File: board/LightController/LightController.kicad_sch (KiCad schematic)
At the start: 34 parts, among them J1 PJ-051AH, J2 Light bank 1, J3 Light Bank 2, J4 Light Bank 3, U1 CPC1002N, U10 CPC1002N, U11 CPC1002N, U12 FeatherS2, U2 CPC1002N, U3 CPC1002N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

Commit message: Add test points.
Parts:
- added TP1: 24V, TestPoint:TestPoint_Pad_D4.0mm, symbol Connector:TestPoint
- added TP2: GND, TestPoint:TestPoint_Loop_D2.54mm_Drill1.5mm_Beaded, symbol Connector:TestPoint
- added TP3: 5V, TestPoint:TestPoint_Pad_D4.0mm, symbol Connector:TestPoint
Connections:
- net +24V: now also TP1.1
- net +5V: now also TP3.1
- net GND: now also TP2.1
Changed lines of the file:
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@@
   (junction (at 44.45 41.91) (diameter 0) (color 0 0 0 0)
   )
+  (junction (at 93.98 59.69) (diameter 0) (color 0 0 0 0)
+  )
   (junction (at 113.03 44.45) (diameter 0) (color 0 0 0 0)
   )
@@
   (junction (at 109.22 44.45) (diameter 0) (color 0 0 0 0)
   )
+  (junction (at 52.07 41.91) (diameter 0) (color 0 0 0 0)
+  )
   (junction (at 87.63 44.45) (diameter 0) (color 0 0 0 0)
+  )
+  (junction (at 116.84 44.45) (diameter 0) (color 0 0 0 0)
   )
   (junction (at 68.58 59.69) (diameter 0) (color 0 0 0 0)
@@
     (stroke (width 0) (type default) (color 0 0 0 0))
   )
+  (wire (pts (xy 52.07 41.91) (xy 54.61 41.91))
+    (stroke (width 0) (type default) (color 0 0 0 0))
+  )
   (wire (pts (xy 109.22 44.45) (xy 109.22 46.99))
     (stroke (width 0) (type default) (color 0 0 0 0))
@@
     (stroke (width 0) (type default) (color 0 0 0 0))
   )
-  (wire (pts (xy 113.03 59.69) (xy 76.2 59.69))
+  (wire (pts (xy 113.03 59.69) (xy 93.98 59.69))
     (stroke (width 0) (type default) (color 0 0 0 0))
   )
@@
     (stroke (width 0) (type default) (color 0 0 0 0))
   )
+  (wire (pts (xy 93.98 59.69) (xy 76.2 59.69))
+    (stroke (width 0) (type default) (color 0 0 0 0))
+  )
   (wire (pts (xy 222.25 92.71) (xy 231.14 92.71))
     (stroke (width 0) (type default) (color 0 0 0 0))
@@
     (stroke (width 0) (type default) (color 0 0 0 0))
   )
-  (wire (pts (xy 113.03 44.45) (xy 123.19 44.45))
+  (wire (pts (xy 113.03 44.45) (xy 116.84 44.45))
     (stroke (width 0) (type default) (color 0 0 0 0))
   )
@@
     (stroke (width 0) (type default) (color 0 0 0 0))
   )
-  (wire (pts (xy 48.26 41.91) (xy 54.61 41.91))
+  (wire (pts (xy 48.26 41.91) (xy 52.07 41.91))
     (stroke (width 0) (type default) (color 0 0 0 0))
   )
@@
   )
   (wire (pts (xy 257.175 55.88) (xy 259.08 55.88))
+    (stroke (width 0) (type default) (color 0 0 0 0))
+  )
+  (wire (pts (xy 116.84 44.45) (xy 123.19 44.45))
     (stroke (width 0) (type default) (color 0 0 0 0))
   )
@@
   (symbol (lib_id "power:GND") (at 240.03 32.385 0) (unit 1)
     (in_bom yes) (on_board yes) (fields_autoplaced)
-    (property "Reference" "#PWR026" (id 0) (at 240.03 38.735 0)
+    (property "Reference" "#PWR027" (id 0) (at 240.03 38.735 0)
       (effects (font (size 1.27 1.27)) hide)
     )
@@
     (pin "2")
   )
+  (symbol (lib_id "Connector:TestPoint") (at 52.07 41.91 0) (unit 1)
+    (in_bom yes) (on_board yes)
+    (property "Reference" "TP1" (id 0) (at 50.8 34.29 0)
+      (effects (font (size 1.27 1.27)) (justify left))
+    )
+    (property "Value" "24V" (id 1) (at 50.8 36.83 0)
+      (effects (font (size 1.27 1.27)) (justify left))
+    )
+    (property "Footprint" "TestPoint:TestPoint_Pad_D4.0mm" (id 2) (at 57.15 41.91 0)
+      (effects (font (size 1.27 1.27)) hide)
+    )
+    (property "Datasheet" "~" (id 3) (at 57.15 41.91 0)
+      (effects (font (size 1.27 1.27)) hide)
+    )
+    (pin "1")
+  )
   (symbol (lib_id "power:GND") (at 21.59 182.88 0) (unit 1)
     (in_bom yes) (on_board yes) (fields_autoplaced)
@@
     )
     (property "Datasheet" "" (id 3) (at 231.14 90.17 0)
+      (effects (font (size 1.27 1.27)) hide)
+    )
+    (pin "1")
+  )
+  (symbol (lib_id "Connector:TestPoint") (at 116.84 44.45 0) (unit 1)
+    (in_bom yes) (on_board yes)
+    (property "Reference" "TP3" (id 0) (at 114.046 36.068 0)
+      (effects (font (size 1.27 1.27)) (justify left))
+    )
+    (property "Value" "5V" (id 1) (at 111.252 38.862 0)
+      (effects (font (size 1.27 1.27)) (justify left))
+    )
+    (property "Footprint" "TestPoint:TestPoint_Pad_D4.0mm" (id 2) (at 121.92 44.45 0)
+      (effects (font (size 1.27 1.27)) hide)
+    )
+    (property "Datasheet" "~" (id 3) (at 121.92 44.45 0)
       (effects (font (size 1.27 1.27)) hide)
     )
@@
   (symbol (lib_id "power:GND") (at 240.665 51.435 0) (unit 1)
     (in_bom yes) (on_board yes) (fields_autoplaced)
-    (property "Reference" "#PWR027" (id 0) (at 240.665 57.785 0)
+    (property "Reference" "#PWR028" (id 0) (at 240.665 57.785 0)
       (effects (font (size 1.27 1.27)) hide)
     )
@@
     )
   )
+  (symbol (lib_id "Connector:TestPoint") (at 93.98 59.69 0) (unit 1)
+    (in_bom yes) (on_board yes) (fields_autoplaced)
+    (property "Reference" "TP2" (id 0) (at 96.52 55.1179 0)
+      (effects (font (size 1.27 1.27)) (justify left))
+    )
+    (property "Value" "GND" (id 1) (at 96.52 57.6579 0)
+      (effects (font (size 1.27 1.27)) (justify left))
+    )
+    (property "Footprint" "TestPoint:TestPoint_Loop_D2.54mm_Drill1.5mm_Beaded" (id 2) (at 99.06 59.69 0)
+      (effects (font (size 1.27 1.27)) hide)
+    )
+    (property "Datasheet" "~" (id 3) (at 99.06 59.69 0)
+      (effects (font (size 1.27 1.27)) hide)
+    )
+    (pin "1")
+  )
   (symbol (lib_id "power:GND") (at 238.125 69.215 0) (unit 1)
     (in_bom yes) (on_board yes) (fields_autoplaced)
-    (property "Reference" "#PWR028" (id 0) (at 238.125 75.565 0)
+    (property "Reference" "#PWR026" (id 0) (at 238.125 75.565 0)
       (effects (font (size 1.27 1.27)) hide)
     )
@@
       (reference "#PWR025") (unit 1) (value "+5V") (footprint "")
     )
+    (path "/ffaa8227-6a33-4a9e-b9b1-1fd1b243401f"
+      (reference "#PWR026") (unit 1) (value "GND") (footprint "")
+    )
     (path "/118363d9-1248-4653-9b45-ceb5f08f9daf"
-      (reference "#PWR026") (unit 1) (value "GND") (footprint "")
+      (reference "#PWR027") (unit 1) (value "GND") (footprint "")
     )
     (path "/7219b893-260e-4790-8a1d-0a840f6f2a4d"
-      (reference "#PWR027") (unit 1) (value "GND") (footprint "")
-    )
-    (path "/ffaa8227-6a33-4a9e-b9b1-1fd1b243401f"
       (reference "#PWR028") (unit 1) (value "GND") (footprint "")
     )
@@
       (reference "R10") (unit 1) (value "3K3") (footprint "Resistor_SMD:R_0805_2012Metric")
     )
+    (path "/25f413c1-7149-4b14-bcd6-9f919a841766"
+      (reference "TP1") (unit 1) (value "24V") (footprint "TestPoint:TestPoint_Pad_D4.0mm")
+    )
+    (path "/ff579e34-65c1-4f50-a33e-b27af09e16ee"
+      (reference "TP2") (unit 1) (value "GND") (footprint "TestPoint:TestPoint_Loop_D2.54mm_Drill1.5mm_Beaded")
+    )
+    (path "/46eb0307-3674-45bc-a7fe-d6adb29b2149"
+      (reference "TP3") (unit 1) (value "5V") (footprint "TestPoint:TestPoint_Pad_D4.0mm")
+    )
     (path "/8f2e333e-0bdc-409e-a046-778d2c85a608"

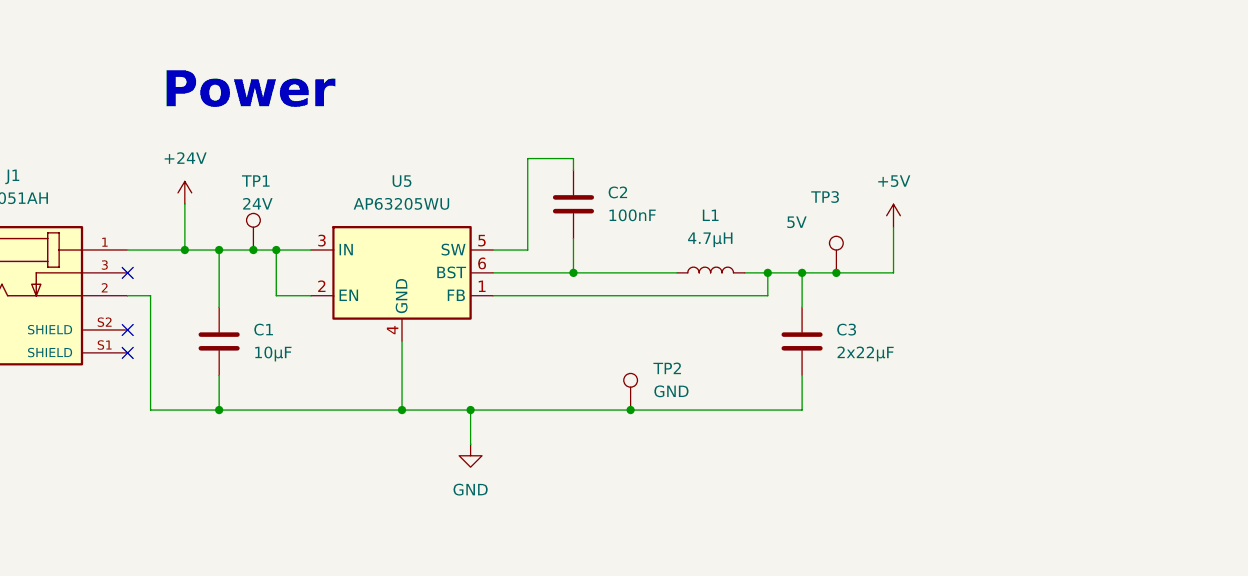
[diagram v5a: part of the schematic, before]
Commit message: Added second parallel bypass cap.
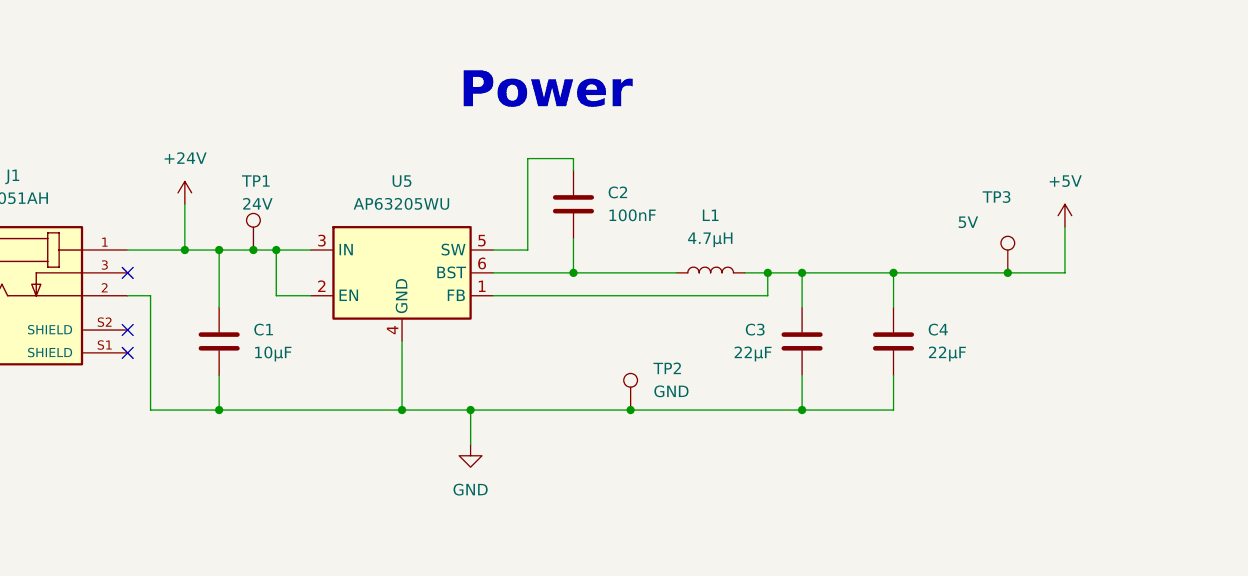
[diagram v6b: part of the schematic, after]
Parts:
- added C4: 22µF, Capacitor_SMD:C_0805_2012Metric, symbol Device:C
- C3: value 2x22µF -> 22µF
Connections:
- net +5V: now also C4.1
- net GND: now also C4.2
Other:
- moved on the sheet: TP3
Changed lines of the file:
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@@
   (junction (at 93.98 59.69) (diameter 0) (color 0 0 0 0)
   )
+  (junction (at 48.26 41.91) (diameter 0) (color 0 0 0 0)
+  )
   (junction (at 113.03 44.45) (diameter 0) (color 0 0 0 0)
   )
-  (junction (at 48.26 41.91) (diameter 0) (color 0 0 0 0)
-  )
   (junction (at 109.22 44.45) (diameter 0) (color 0 0 0 0)
   )
@@
   (junction (at 87.63 44.45) (diameter 0) (color 0 0 0 0)
   )
-  (junction (at 116.84 44.45) (diameter 0) (color 0 0 0 0)
+  (junction (at 113.03 59.69) (diameter 0) (color 0 0 0 0)
+  )
+  (junction (at 135.89 44.45) (diameter 0) (color 0 0 0 0)
   )
   (junction (at 68.58 59.69) (diameter 0) (color 0 0 0 0)
+  )
+  (junction (at 123.19 44.45) (diameter 0) (color 0 0 0 0)
   )
   (junction (at 48.26 59.69) (diameter 0) (color 0 0 0 0)
@@
     (stroke (width 0) (type default) (color 0 0 0 0))
   )
+  (wire (pts (xy 123.19 59.69) (xy 113.03 59.69))
+    (stroke (width 0) (type default) (color 0 0 0 0))
+  )
   (wire (pts (xy 44.45 36.83) (xy 44.45 41.91))
     (stroke (width 0) (type default) (color 0 0 0 0))
@@
     (stroke (width 0) (type default) (color 0 0 0 0))
   )
+  (wire (pts (xy 123.19 55.88) (xy 123.19 59.69))
+    (stroke (width 0) (type default) (color 0 0 0 0))
+  )
   (wire (pts (xy 44.45 41.91) (xy 48.26 41.91))
     (stroke (width 0) (type default) (color 0 0 0 0))
@@
     (stroke (width 0) (type default) (color 0 0 0 0))
   )
+  (wire (pts (xy 123.19 44.45) (xy 123.19 48.26))
+    (stroke (width 0) (type default) (color 0 0 0 0))
+  )
   (wire (pts (xy 257.175 69.85) (xy 259.08 69.85))
     (stroke (width 0) (type default) (color 0 0 0 0))
@@
     (stroke (width 0) (type default) (color 0 0 0 0))
   )
-  (wire (pts (xy 123.19 39.37) (xy 123.19 44.45))
+  (wire (pts (xy 142.24 39.37) (xy 142.24 44.45))
     (stroke (width 0) (type default) (color 0 0 0 0))
   )
@@
     (stroke (width 0) (type default) (color 0 0 0 0))
   )
-  (wire (pts (xy 113.03 44.45) (xy 116.84 44.45))
+  (wire (pts (xy 113.03 44.45) (xy 123.19 44.45))
     (stroke (width 0) (type default) (color 0 0 0 0))
   )
@@
     (stroke (width 0) (type default) (color 0 0 0 0))
   )
-  (wire (pts (xy 116.84 44.45) (xy 123.19 44.45))
+  (wire (pts (xy 135.89 44.45) (xy 142.24 44.45))
     (stroke (width 0) (type default) (color 0 0 0 0))
   )
@@
   )
   (wire (pts (xy 22.225 160.655) (xy 22.225 161.29))
+    (stroke (width 0) (type default) (color 0 0 0 0))
+  )
+  (wire (pts (xy 123.19 44.45) (xy 135.89 44.45))
     (stroke (width 0) (type default) (color 0 0 0 0))
   )
@@
     (effects (font (size 4 4) (thickness 0.8) bold) (justify left bottom))
   )
-  (text "Power" (at 41.91 26.67 0)
+  (text "Power" (at 74.93 26.67 0)
     (effects (font (size 4 4) (thickness 0.8) bold) (justify left bottom))
   )
@@
   )
   (symbol (lib_id "Device:C") (at 113.03 52.07 0) (unit 1)
-    (in_bom yes) (on_board yes) (fields_autoplaced)
-    (property "Reference" "C3" (id 0) (at 116.84 50.7999 0)
-      (effects (font (size 1.27 1.27)) (justify left))
-    )
-    (property "Value" "2x22µF" (id 1) (at 116.84 53.3399 0)
+    (in_bom yes) (on_board yes)
+    (property "Reference" "C3" (id 0) (at 106.68 50.8 0)
+      (effects (font (size 1.27 1.27)) (justify left))
+    )
+    (property "Value" "22µF" (id 1) (at 105.41 53.34 0)
       (effects (font (size 1.27 1.27)) (justify left))
     )
@@
     (pin "1")
   )
-  (symbol (lib_id "Connector:TestPoint") (at 116.84 44.45 0) (unit 1)
+  (symbol (lib_id "Connector:TestPoint") (at 135.89 44.45 0) (unit 1)
     (in_bom yes) (on_board yes)
-    (property "Reference" "TP3" (id 0) (at 114.046 36.068 0)
-      (effects (font (size 1.27 1.27)) (justify left))
-    )
-    (property "Value" "5V" (id 1) (at 111.252 38.862 0)
-      (effects (font (size 1.27 1.27)) (justify left))
-    )
-    (property "Footprint" "TestPoint:TestPoint_Pad_D4.0mm" (id 2) (at 121.92 44.45 0)
-      (effects (font (size 1.27 1.27)) hide)
-    )
-    (property "Datasheet" "~" (id 3) (at 121.92 44.45 0)
+    (property "Reference" "TP3" (id 0) (at 133.096 36.068 0)
+      (effects (font (size 1.27 1.27)) (justify left))
+    )
+    (property "Value" "5V" (id 1) (at 130.302 38.862 0)
+      (effects (font (size 1.27 1.27)) (justify left))
+    )
+    (property "Footprint" "TestPoint:TestPoint_Pad_D4.0mm" (id 2) (at 140.97 44.45 0)
+      (effects (font (size 1.27 1.27)) hide)
+    )
+    (property "Datasheet" "~" (id 3) (at 140.97 44.45 0)
       (effects (font (size 1.27 1.27)) hide)
     )
@@
     (pin "1")
   )
-  (symbol (lib_id "power:+5V") (at 123.19 39.37 0) (unit 1)
-    (in_bom yes) (on_board yes) (fields_autoplaced)
-    (property "Reference" "#PWR020" (id 0) (at 123.19 43.18 0)
-      (effects (font (size 1.27 1.27)) hide)
-    )
-    (property "Value" "+5V" (id 1) (at 123.19 34.29 0))
-    (property "Footprint" "" (id 2) (at 123.19 39.37 0)
-      (effects (font (size 1.27 1.27)) hide)
-    )
-    (property "Datasheet" "" (id 3) (at 123.19 39.37 0)
+  (symbol (lib_id "power:+5V") (at 142.24 39.37 0) (unit 1)
+    (in_bom yes) (on_board yes) (fields_autoplaced)
+    (property "Reference" "#PWR020" (id 0) (at 142.24 43.18 0)
+      (effects (font (size 1.27 1.27)) hide)
+    )
+    (property "Value" "+5V" (id 1) (at 142.24 34.29 0))
+    (property "Footprint" "" (id 2) (at 142.24 39.37 0)
+      (effects (font (size 1.27 1.27)) hide)
+    )
+    (property "Datasheet" "" (id 3) (at 142.24 39.37 0)
       (effects (font (size 1.27 1.27)) hide)
     )
@@
       (effects (font (size 1.27 1.27)) hide)
     )
+  )
+  (symbol (lib_id "Device:C") (at 123.19 52.07 0) (unit 1)
+    (in_bom yes) (on_board yes) (fields_autoplaced)
+    (property "Reference" "C4" (id 0) (at 127 50.7999 0)
+      (effects (font (size 1.27 1.27)) (justify left))
+    )
+    (property "Value" "22µF" (id 1) (at 127 53.3399 0)
+      (effects (font (size 1.27 1.27)) (justify left))
+    )
+    (property "Footprint" "Capacitor_SMD:C_0805_2012Metric" (id 2) (at 124.1552 55.88 0)
+      (effects (font (size 1.27 1.27)) hide)
+    )
+    (property "Datasheet" "~" (id 3) (at 123.19 52.07 0)
+      (effects (font (size 1.27 1.27)) hide)
+    )
+    (pin "1")
+    (pin "2")
   )
   (symbol (lib_id "Relay_SolidState:CPC1002N") (at 38.735 179.705 0) (unit 1)
@@
     )
     (path "/358be4dc-9ae7-42fb-bb5f-97253842315f"
-      (reference "C3") (unit 1) (value "2x22µF") (footprint "Capacitor_SMD:C_0805_2012Metric")
+      (reference "C3") (unit 1) (value "22µF") (footprint "Capacitor_SMD:C_0805_2012Metric")
+    )
+    (path "/8da86106-0751-4439-acdd-3f37b2dbfba6"
+      (reference "C4") (unit 1) (value "22µF") (footprint "Capacitor_SMD:C_0805_2012Metric")
     )
     (path "/5fdabda6-9c9c-427b-87e5-a291030a9854"

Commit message: fixed resistor label orientations.
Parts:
- L1: value 4.7µH -> 8.7µH
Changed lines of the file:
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@@
   (symbol (lib_id "Device:R") (at 76.835 137.16 90) (unit 1)
     (in_bom yes) (on_board yes)
-    (property "Reference" "R6" (id 0) (at 76.2 142.875 0)
-      (effects (font (size 1.27 1.27)) (justify left))
-    )
-    (property "Value" "3K3" (id 1) (at 78.105 142.875 0)
+    (property "Reference" "R6" (id 0) (at 78.74 139.7 90)
+      (effects (font (size 1.27 1.27)) (justify left))
+    )
+    (property "Value" "3K3" (id 1) (at 80.01 142.24 90)
       (effects (font (size 1.27 1.27)) (justify left))
     )
@@
   (symbol (lib_id "Device:R") (at 77.47 102.87 90) (unit 1)
     (in_bom yes) (on_board yes)
-    (property "Reference" "R7" (id 0) (at 76.835 108.585 0)
-      (effects (font (size 1.27 1.27)) (justify left))
-    )
-    (property "Value" "3K3" (id 1) (at 78.74 108.585 0)
+    (property "Reference" "R7" (id 0) (at 78.74 105.41 90)
+      (effects (font (size 1.27 1.27)) (justify left))
+    )
+    (property "Value" "3K3" (id 1) (at 80.01 107.95 90)
       (effects (font (size 1.27 1.27)) (justify left))
     )
@@
     (in_bom yes) (on_board yes) (fields_autoplaced)
     (property "Reference" "L1" (id 0) (at 102.87 38.1 90))
-    (property "Value" "4.7µH" (id 1) (at 102.87 40.64 90))
+    (property "Value" "8.7µH" (id 1) (at 102.87 40.64 90))
     (property "Footprint" "Inductor_SMD:L_0805_2012Metric" (id 2) (at 102.87 44.45 0)
       (effects (font (size 1.27 1.27)) hide)
@@
   (symbol (lib_id "Device:R") (at 124.46 161.925 90) (unit 1)
     (in_bom yes) (on_board yes)
-    (property "Reference" "R8" (id 0) (at 123.825 167.64 0)
-      (effects (font (size 1.27 1.27)) (justify left))
-    )
-    (property "Value" "3K3" (id 1) (at 125.73 167.64 0)
+    (property "Reference" "R8" (id 0) (at 127 165.1 90)
+      (effects (font (size 1.27 1.27)) (justify left))
+    )
+    (property "Value" "3K3" (id 1) (at 128.27 167.64 90)
       (effects (font (size 1.27 1.27)) (justify left))
     )
@@
   (symbol (lib_id "Device:R") (at 76.2 161.925 90) (unit 1)
     (in_bom yes) (on_board yes)
-    (property "Reference" "R5" (id 0) (at 75.565 167.64 0)
-      (effects (font (size 1.27 1.27)) (justify left))
-    )
-    (property "Value" "3K3" (id 1) (at 77.47 167.64 0)
+    (property "Reference" "R5" (id 0) (at 78.74 165.1 90)
+      (effects (font (size 1.27 1.27)) (justify left))
+    )
+    (property "Value" "3K3" (id 1) (at 80.01 167.64 90)
       (effects (font (size 1.27 1.27)) (justify left))
     )
@@
   (symbol (lib_id "Device:R") (at 125.095 137.16 90) (unit 1)
     (in_bom yes) (on_board yes)
-    (property "Reference" "R9" (id 0) (at 124.46 142.875 0)
-      (effects (font (size 1.27 1.27)) (justify left))
-    )
-    (property "Value" "3K3" (id 1) (at 126.365 142.875 0)
+    (property "Reference" "R9" (id 0) (at 127 139.7 90)
+      (effects (font (size 1.27 1.27)) (justify left))
+    )
+    (property "Value" "3K3" (id 1) (at 128.27 142.24 90)
       (effects (font (size 1.27 1.27)) (justify left))
     )
@@
   (symbol (lib_id "Device:R") (at 26.67 160.655 90) (unit 1)
     (in_bom yes) (on_board yes)
-    (property "Reference" "R2" (id 0) (at 26.035 166.37 0)
-      (effects (font (size 1.27 1.27)) (justify left))
-    )
-    (property "Value" "3K3" (id 1) (at 27.94 166.37 0)
+    (property "Reference" "R2" (id 0) (at 27.94 163.83 90)
+      (effects (font (size 1.27 1.27)) (justify left))
+    )
+    (property "Value" "3K3" (id 1) (at 29.21 166.37 90)
       (effects (font (size 1.27 1.27)) (justify left))
     )
@@
   (symbol (lib_id "Device:R") (at 27.305 135.89 90) (unit 1)
     (in_bom yes) (on_board yes)
-    (property "Reference" "R3" (id 0) (at 26.67 141.605 0)
-      (effects (font (size 1.27 1.27)) (justify left))
-    )
-    (property "Value" "3K3" (id 1) (at 28.575 141.605 0)
+    (property "Reference" "R3" (id 0) (at 29.21 138.43 90)
+      (effects (font (size 1.27 1.27)) (justify left))
+    )
+    (property "Value" "3K3" (id 1) (at 30.48 140.97 90)
       (effects (font (size 1.27 1.27)) (justify left))
     )
@@
   (symbol (lib_id "Device:R") (at 26.035 182.245 90) (unit 1)
     (in_bom yes) (on_board yes)
-    (property "Reference" "R1" (id 0) (at 25.4 187.96 0)
-      (effects (font (size 1.27 1.27)) (justify left))
-    )
-    (property "Value" "3K3" (id 1) (at 27.305 187.96 0)
+    (property "Reference" "R1" (id 0) (at 27.94 185.42 90)
+      (effects (font (size 1.27 1.27)) (justify left))
+    )
+    (property "Value" "3K3" (id 1) (at 29.21 187.96 90)
       (effects (font (size 1.27 1.27)) (justify left))
     )
@@
   (symbol (lib_id "Device:R") (at 127 104.14 90) (unit 1)
     (in_bom yes) (on_board yes)
-    (property "Reference" "R10" (id 0) (at 126.365 109.855 0)
-      (effects (font (size 1.27 1.27)) (justify left))
-    )
-    (property "Value" "3K3" (id 1) (at 128.27 109.855 0)
+    (property "Reference" "R10" (id 0) (at 129.54 106.68 90)
+      (effects (font (size 1.27 1.27)) (justify left))
+    )
+    (property "Value" "3K3" (id 1) (at 129.54 109.22 90)
       (effects (font (size 1.27 1.27)) (justify left))
     )
@@
     )
     (path "/4af9f695-9d31-47b7-9c1e-fff616a0e148"
-      (reference "L1") (unit 1) (value "4.7µH") (footprint "Inductor_SMD:L_0805_2012Metric")
+      (reference "L1") (unit 1) (value "8.7µH") (footprint "Inductor_SMD:L_0805_2012Metric")
     )
     (path "/d450be2c-5607-4e49-82b4-991878978321"
